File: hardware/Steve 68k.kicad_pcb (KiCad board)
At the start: 2 copper layers, 99 x 98.9 mm, 49 parts, among them IC1 MC68008FN12F, J1 Serial 1, J2 Conn_02x32_Odd_Even, J3 Conn_01x03_Male, J4 Conn_01x02_Male, J5 Conn_01x10, J6 Conn_01x10, J7 Serial 2, SW1 Reset, U1 74LS32, U2 SST39SF040, U3 74LS257, U4 74HC04, U5 MC68681FN, U6 74LS138, U7 AS6C4008-55PCN, U8 Max705, X1 4.0Mhz, X2 1.8432 Mhz

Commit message: Serial Test and some changes to the PCB
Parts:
- removed C13: .1uF, Capacitor_SMD:C_0603_1608Metric
- added R11: 10k, Resistor_SMD:R_0603_1608Metric, F.Cu at (105.5, 60.0)
- added R12: 10k, Resistor_SMD:R_0603_1608Metric, F.Cu at (105.5, 63.6)
- added R13: 10k, Resistor_SMD:R_0603_1608Metric, F.Cu at (105.5, 67.3)
- IC1: value MC68008FN12F -> MC68008FN8
- SW1: footprint Button_Switch_SMD:SW_Push_1P1T_NO_6x6mm_H9.5mm -> Button_Switch_THT:SW_PUSH_6mm
- U1, U4: footprint Package_DIP:DIP-14_W7.62mm_Socket_LongPads -> Package_SO:SOIC-14_3.9x8.7mm_P1.27mm
- U2: value SST39SF040 -> 28C256; footprint Package_LCC:PLCC-32_THT-Socket -> Package_DIP:DIP-28_W15.24mm_Socket_LongPads
- U6: footprint Package_DIP:DIP-16_W7.62mm_Socket_LongPads -> Package_SO:SOIC-16_3.9x9.9mm_P1.27mm
- U7: footprint Package_DIP:DIP-32_W15.24mm_Socket_LongPads -> Package_SO:SSOP-32_11.305x20.495mm_P1.27mm
- X1: value 4.0Mhz -> CXO_DIP8
- moved C10 79.5 mm to (97.8, 70.9), turned to 0 degrees
- moved C6 70.9 mm to (93.5, 89.0), turned to -90 degrees
- moved C4 68.6 mm to (135.8, 106.7), turned to 90 degrees
- moved J3 67.6 mm to (125.7, 75.3)
- moved C9 58.0 mm to (144.1, 39.2)
- moved X1 56.6 mm to (128.2, 110.5), turned to 90 degrees
- moved J4 54.7 mm to (125.7, 86.2)
- moved C11 44.6 mm to (114.5, 70.9), turned to 0 degrees
- moved C1 39.6 mm to (106.2, 70.9)
- moved C7 38.0 mm to (102.0, 92.9)
- moved C8 35.8 mm to (122.7, 39.2)
- moved C2 34.6 mm to (88.2, 38.9)
- moved C3 32.7 mm to (116.5, 106.6)
- moved U3 27.9 mm to (132.8, 75.0)
- moved U6 23.9 mm to (106.2, 78.5)
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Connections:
- net Net-(X2-Pad8) renamed /UART_CLK
- IC1 pad 36: VCC -> /~{BGACK}
- IC1 pad 37: VCC -> /~{BR}
- IC1 pad 44: VCC -> /~{BERR}
- J2 pad 38: VCC -> /~{BERR}
- J2 pad 47: VCC -> /~{BR}
- J2 pad 48: VCC -> /~{BGACK}
- U2 pad 1: /A18 -> /A14
- U2 pad 10: /A2 -> /A0
- U2 pad 11: /A1 -> /D0
- U2 pad 12: /A0 -> /D1
- U2 pad 13: /D0 -> /D2
- U2 pad 14: /D1 -> GND
- U2 pad 15: /D2 -> /D3
- U2 pad 16: GND -> /D4
- U2 pad 17: /D3 -> /D5
- U2 pad 18: /D4 -> /D6
- U2 pad 19: /D5 -> /D7
- U2 pad 2: /A16 -> /A12
- U2 pad 20: /D6 -> /~{ROMSEL}
- U2 pad 21: /D7 -> /A10
- U2 pad 22: /~{ROMSEL} -> /~{OE}
- U2 pad 23: /A10 -> /A11
- U2 pad 24: /~{OE} -> /A9
- U2 pad 25: /A11 -> /A8
- U2 pad 26: /A9 -> /A13
- U2 pad 27: /A8 -> VCC
- U2 pad 28: /A13 -> VCC
- U2 pad 3: /A15 -> /A7
- U2 pad 4: /A12 -> /A6
- U2 pad 5: /A7 -> /A5
- U2 pad 6: /A6 -> /A4
- U2 pad 7: /A5 -> /A3
- U2 pad 8: /A4 -> /A2
- U2 pad 9: /A3 -> /A1
- U3 pad 15: VCC -> GND
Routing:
- net GND: track 530.2 -> 0.00 mm, vias 2 -> 0
- net VCC: track 484.9 -> 0.00 mm, vias 2 -> 0
- net /A1: track 230.5 -> 0.00 mm, vias 1 -> 0
- net /A3: track 213.7 -> 0.00 mm, vias 1 -> 0
- net /A0: track 213.5 -> 0.00 mm, vias 2 -> 0
- net /A2: track 198.1 -> 0.00 mm, vias 1 -> 0
- net /D4: track 192.2 -> 0.00 mm
- net /~{IPL0}: track 190.1 -> 0.00 mm
- net /D6: track 180.8 -> 0.00 mm
- net /D0: track 179.9 -> 0.00 mm, vias 2 -> 0
- net /FC1: track 177.9 -> 0.00 mm
- net /~{RESET}: track 173.7 -> 0.00 mm, vias 2 -> 0
- net /A20: track 170.9 -> 0.00 mm, vias 1 -> 0
- net /68681_Int: track 165.6 -> 0.00 mm
- net /D2: track 165.5 -> 0.00 mm, vias 2 -> 0
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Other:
- board text added: "Clk"
- board text added: "RX"
- board text added: "TX"
- board text added: "V20220518"
- board text added: "VCC"
- board text removed: "V20220503"

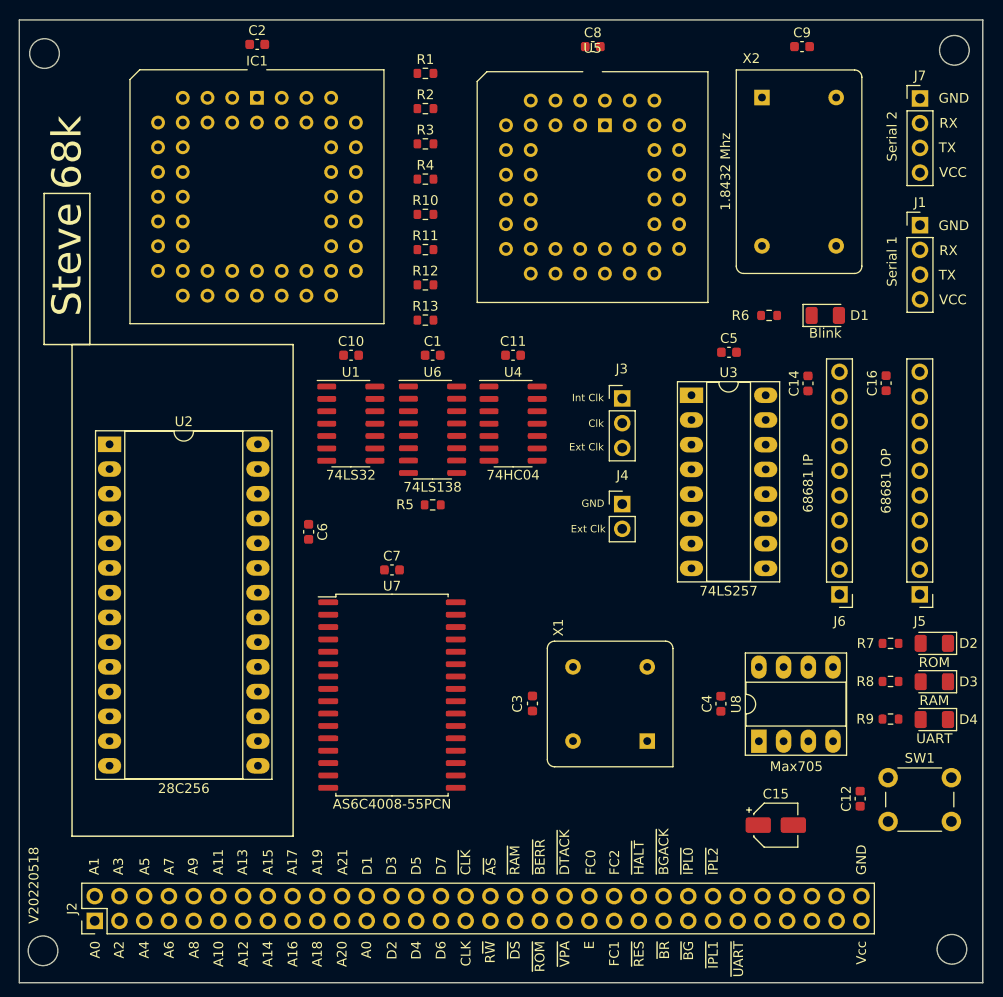
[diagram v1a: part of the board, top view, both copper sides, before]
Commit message: Working on PLD for Glue Logic
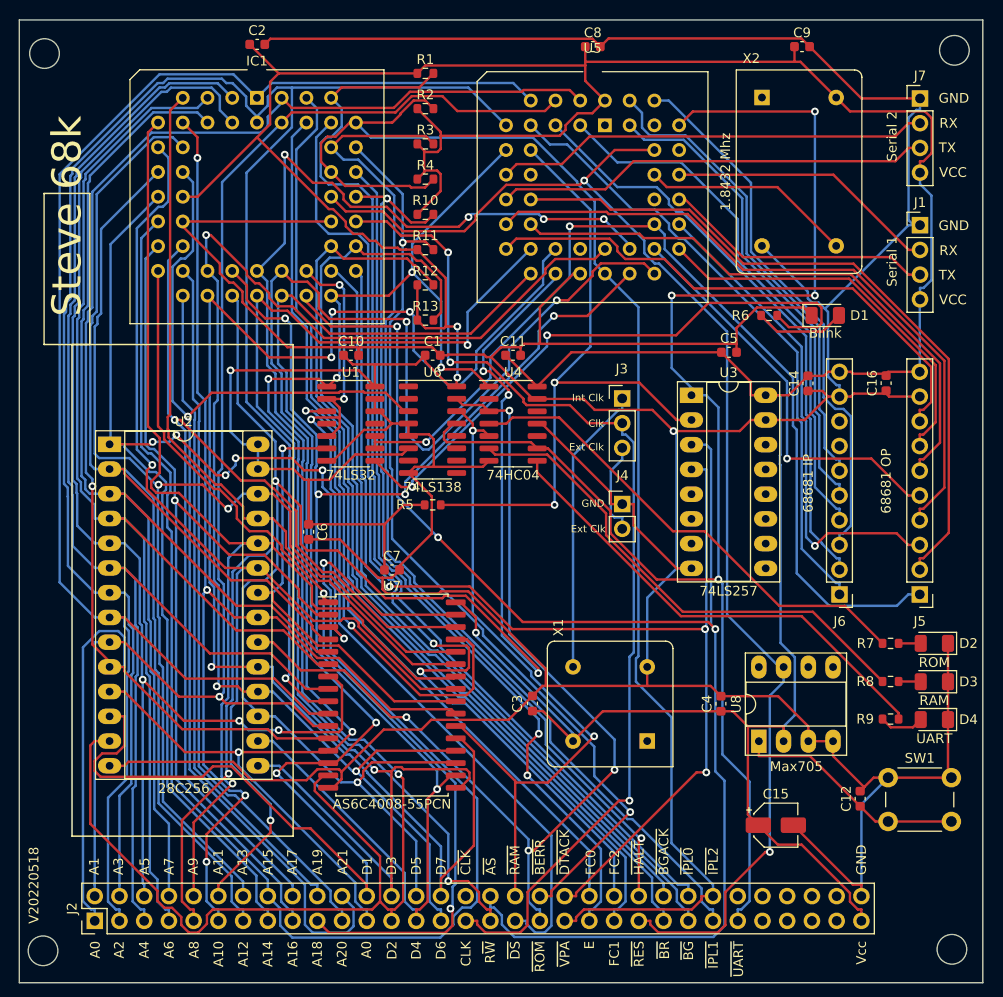
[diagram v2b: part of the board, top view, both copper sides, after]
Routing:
- net GND: track 0.00 -> 539.4 mm, vias 0 -> 1
- net VCC: track 0.00 -> 457.3 mm, vias 0 -> 4
- net /A3: track 0.00 -> 204.9 mm, vias 0 -> 1
- net /D2: track 0.00 -> 194.5 mm, vias 0 -> 5
- net /D5: track 0.00 -> 172.1 mm, vias 0 -> 5
- net /A0: track 0.00 -> 171.5 mm, vias 0 -> 1
- net /D0: track 0.00 -> 166.0 mm, vias 0 -> 4
- net /A2: track 0.00 -> 164.6 mm
- net /A15: track 0.00 -> 159.2 mm, vias 0 -> 1
- net /~{UARTSEL}: track 0.00 -> 155.5 mm, vias 0 -> 4
- net /D1: track 0.00 -> 151.0 mm, vias 0 -> 2
- net /D7: track 0.00 -> 150.9 mm, vias 0 -> 4
- net /D4: track 0.00 -> 150.0 mm, vias 0 -> 5
- net /68681_Int: track 0.00 -> 150.0 mm
- net /A1: track 0.00 -> 146.0 mm, vias 0 -> 1
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
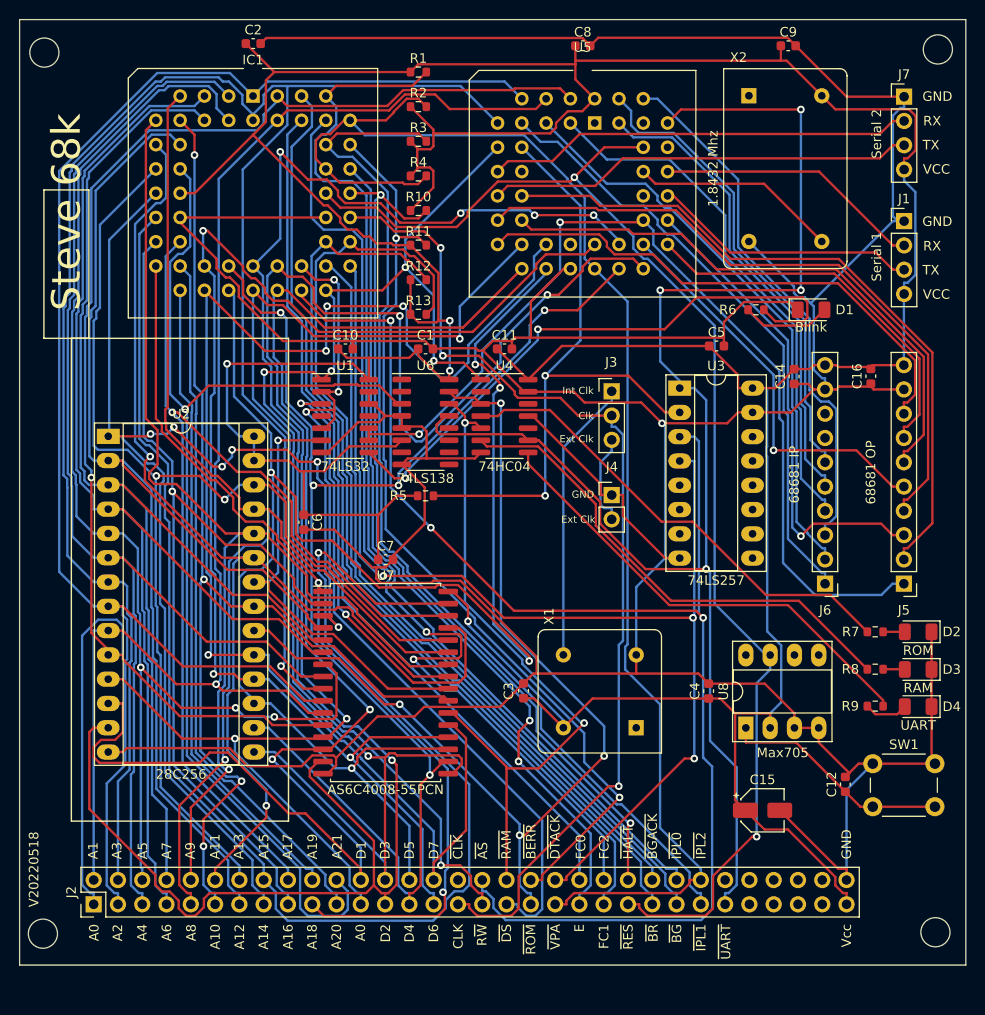
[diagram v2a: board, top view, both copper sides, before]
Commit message: New version of PCB using a GAL
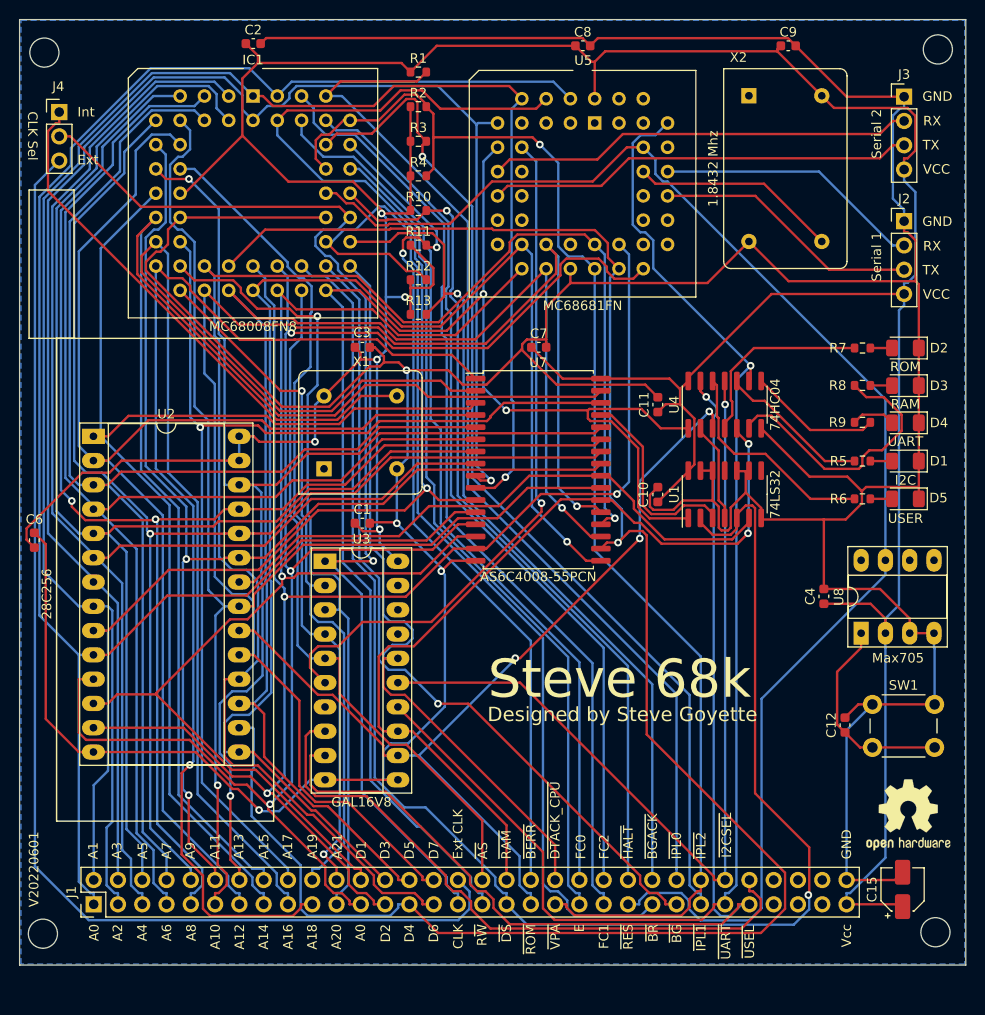
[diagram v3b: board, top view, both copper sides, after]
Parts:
- removed C14, C16, C5: .1uF, Capacitor_SMD:C_0603_1608Metric
- removed the J4 at (125.7, 86.2)
- removed J5, J6: Conn_01x10, Connector_PinHeader_2.54mm:PinHeader_1x10_P2.54mm_Vertical
- removed U6: 74LS138, Package_SO:SOIC-16_3.9x9.9mm_P1.27mm
- added D5: USER, LED_SMD:LED_1206_3216Metric, F.Cu at (156.4, 86.5)
- added REF**: OSHW-Logo2_9.8x8mm_SilkScreen, Symbol:OSHW-Logo2_9.8x8mm_SilkScreen, F.Cu at (156.7, 119.6)
- D1: value Blink -> I2C
- R5: value 10k -> 220
- U3: value 74LS257 -> GAL16V8; footprint Package_DIP:DIP-16_W7.62mm_Socket_LongPads -> Package_DIP:DIP-20_W7.62mm_Socket_LongPads
- moved J4 64.7 mm to (67.9, 46.1)
- moved R5 45.8 mm to (151.9, 82.6), turned to 0 degrees
- moved X1 42.4 mm to (95.6, 83.4), turned to 0 degrees
- moved U3 41.3 mm to (95.7, 93.1)
- moved U1 40.5 mm to (137.5, 86.1), turned to 90 degrees
- moved C3 39.7 mm to (99.6, 70.7), turned to 0 degrees
- moved C10 36.0 mm to (130.5, 86.1), turned to 90 degrees
- moved D2 29.7 mm to (156.4, 70.8)
- moved D3 29.7 mm to (156.4, 74.7)
- moved D4 29.7 mm to (156.4, 78.6)
- moved R7 29.7 mm to (151.9, 70.8)
- moved R8 29.7 mm to (151.9, 74.7)
- moved R9 29.7 mm to (151.9, 78.5)
- moved C6 28.2 mm to (65.3, 90.9), turned to 90 degrees
- moved U7 27.4 mm to (118.0, 83.5)
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- renumbered J2 to J1, J1 to J2, J7 to J3, J3 to J4
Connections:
- IC1 pad 34: /~{CPU_DTACK} -> /~{DTACK_CPU}
- J1 pad 32: /~{CLK} -> /CLK_EXTERNAL
- J1 pad 40: /~{CPU_DTACK} -> /~{DTACK_CPU}
- J1 pad 54: /RES1 -> /~{I2CSEL}
- J1 pad 55: /RES2 -> /~{USERSEL}
- J1 pad 56: /RES3 -> /~{DTACK_USER}
- J1 pad 57: /RES4 -> unconnected-(J1-Pad57)
- J1 pad 58: /RES5 -> unconnected-(J1-Pad58)
- J1 pad 59: /RES6 -> unconnected-(J1-Pad59)
- J1 pad 60: /RES7 -> unconnected-(J1-Pad60)
- J1 pad 61: /RES8 -> unconnected-(J1-Pad61)
- J1 pad 62: /RES9 -> unconnected-(J1-Pad62)
- R5 pad 1: /~{DTACK_UART} -> Net-(U4-Pad10)
- R5 pad 2: VCC -> Net-(D1-Pad2)
- R6 pad 1: Net-(R6-Pad1) -> Net-(U4-Pad12)
- R6 pad 2: Net-(D1-Pad2) -> Net-(D5-Pad2)
- U1 pad 10: /OP0 -> GND
- U1 pad 8: Net-(R6-Pad1) -> unconnected-(U1-Pad8)
- U1 pad 9: /OP0 -> GND
- U3 pad 1: /~{UARTSEL} -> /CLK
- U3 pad 10: unconnected-(U3-Pad10) -> GND
- U3 pad 11: unconnected-(U3-Pad11) -> GND
- U3 pad 12: unconnected-(U3-Pad12) -> /~{ROMSEL}
- U3 pad 13: unconnected-(U3-Pad13) -> /~{RAMSEL}
- U3 pad 14: unconnected-(U3-Pad14) -> /~{UARTSEL}
- U3 pad 15: GND -> /~{I2CSEL}
- U3 pad 16: VCC -> /~{DTACK_CPU}
- U3 pad 2: /~{DTACK_UART} -> /A19
- U3 pad 3: /~{AS} -> /A20
- U3 pad 4: /~{CPU_DTACK} -> /A21
- U3 pad 5: unconnected-(U3-Pad5) -> /~{AS}
- U3 pad 6: unconnected-(U3-Pad6) -> /~{DTACK_UART}
- U3 pad 7: unconnected-(U3-Pad7) -> /DTACK_I2C
- U3 pad 8: GND -> /~{DTACK_USER}
- U3 pad 9: unconnected-(U3-Pad9) -> /~{USERSEL}
- U4 pad 10: unconnected-(U4-Pad10) -> Net-(U4-Pad10)
- U4 pad 11: GND -> /~{I2CSEL}
- U4 pad 12: unconnected-(U4-Pad12) -> Net-(U4-Pad12)
- U4 pad 13: GND -> /~{USERSEL}
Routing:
- net /~{CPU_DTACK}: track 121.1 -> 0.00 mm, vias 3 -> 0
- net /~{USERSEL}: track 0.00 -> 119.4 mm, vias 0 -> 1
- net /CLK_EXTERNAL: track 9.76 -> 126.6 mm
- net /OP0: track 100.0 -> 0.00 mm, vias 2 -> 0
- net /~{I2CSEL}: track 0.00 -> 95.2 mm, vias 0 -> 1
- net /~{DTACK_CPU}: track 0.00 -> 81.3 mm
- net /OP1: track 72.8 -> 0.00 mm
- net /~{AS}: track 146.0 -> 73.3 mm, vias 3 -> 0
- net /~{DS}: track 92.8 -> 164.6 mm, vias 3 -> 1
- net /OP3: track 69.5 -> 0.00 mm
- net /~{DTACK_USER}: track 0.00 -> 66.8 mm
- net /IP0: track 64.2 -> 0.00 mm
- net Net-(R6-Pad1): track 62.9 -> 0.00 mm, vias 2 -> 0
- net /IP1: track 60.6 -> 0.00 mm
- net /OP5: track 60.1 -> 0.00 mm
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- added copper zone on B.Cu, net GND
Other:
- board text added: "CLK Sel"
- board text added: "Designed by Steve Goyette"
- board text added: "Ext"
- board text added: "Ext CLK"
- board text added: "Int"
- board text added: "V20220601"
- board text added: "~{DTACK_CPU}"
- board text added: "~{I2CSEL}"
- board text added: "~{USEL}"
- board text removed: "68681 IP"
- board text removed: "68681 OP"
- board text removed: "Clk"
- board text removed: "Ext Clk"
- board text removed: "Int Clk"
- board text removed: "V20220518"
- board text removed: "~{CLK}"
- board text removed: "~{DTACK}"

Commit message: Rev V20220601
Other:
- board text added: "D0"
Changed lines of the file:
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@@
     (fp_line (start -1.33 0) (end -1.33 -1.33) (layer "F.SilkS") (width 0.12))
     (fp_line (start -1.33 -1.33) (end 0 -1.33) (layer "F.SilkS") (width 0.12))
-    (fp_line (start -1.33 1.27) (end 1.33 1.27) (layer "F.SilkS") (width 0.12))
     (fp_line (start 1.33 1.27) (end 1.33 8.95) (layer "F.SilkS") (width 0.12))
+    (fp_line (start -1.33 1.27) (end 1.33 1.27) (layer "F.SilkS") (width 0.12))
     (fp_line (start -1.8 9.4) (end 1.8 9.4) (layer "F.CrtYd") (width 0.05))
     (fp_line (start 1.8 9.4) (end 1.8 -1.8) (layer "F.CrtYd") (width 0.05))
@@
     (fp_line (start -0.14058 0.51) (end 0.14058 0.51) (layer "F.SilkS") (width 0.12))
     (fp_line (start -0.14058 -0.51) (end 0.14058 -0.51) (layer "F.SilkS") (width 0.12))
-    (fp_line (start 1.48 0.73) (end -1.48 0.73) (layer "F.CrtYd") (width 0.05))
-    (fp_line (start 1.48 -0.73) (end 1.48 0.73) (layer "F.CrtYd") (width 0.05))
     (fp_line (start -1.48 0.73) (end -1.48 -0.73) (layer "F.CrtYd") (width 0.05))
     (fp_line (start -1.48 -0.73) (end 1.48 -0.73) (layer "F.CrtYd") (width 0.05))
-    (fp_line (start 0.8 0.4) (end -0.8 0.4) (layer "F.Fab") (width 0.1))
-    (fp_line (start -0.8 0.4) (end -0.8 -0.4) (layer "F.Fab") (width 0.1))
+    (fp_line (start 1.48 -0.73) (end 1.48 0.73) (layer "F.CrtYd") (width 0.05))
+    (fp_line (start 1.48 0.73) (end -1.48 0.73) (layer "F.CrtYd") (width 0.05))
     (fp_line (start 0.8 -0.4) (end 0.8 0.4) (layer "F.Fab") (width 0.1))
     (fp_line (start -0.8 -0.4) (end 0.8 -0.4) (layer "F.Fab") (width 0.1))
+    (fp_line (start -0.8 0.4) (end -0.8 -0.4) (layer "F.Fab") (width 0.1))
+    (fp_line (start 0.8 0.4) (end -0.8 0.4) (layer "F.Fab") (width 0.1))
     (pad "1" smd roundrect (at -0.775 0) (size 0.9 0.95) (layers "F.Cu" "F.Paste" "F.Mask") (roundrect_rratio 0.25)
       (net 1 "VCC") (pintype "passive"))
@@
     (effects (font (size 1 1) (thickness 0.15)))
   )
-  (gr_text "A0" (at 99.4156 131.0132 90) (layer "F.SilkS")
+  (gr_text "D0" (at 99.4156 131.0132 90) (layer "F.SilkS")
     (effects (font (size 1 1) (thickness 0.15)) (justify right))
   )
